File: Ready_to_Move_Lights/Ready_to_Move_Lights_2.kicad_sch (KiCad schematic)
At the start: 42 parts, among them IC1 TLV2371QDBVRQ1, J1 PET-02-XX-X-VT-LC, J2 776280-1, K1 VORA1150-X017T, Q1 IRLZ44N, U1 LM393LVQDDFRQ1, U2 PAMC0381D10QDFXRQ1, U3 NE555D

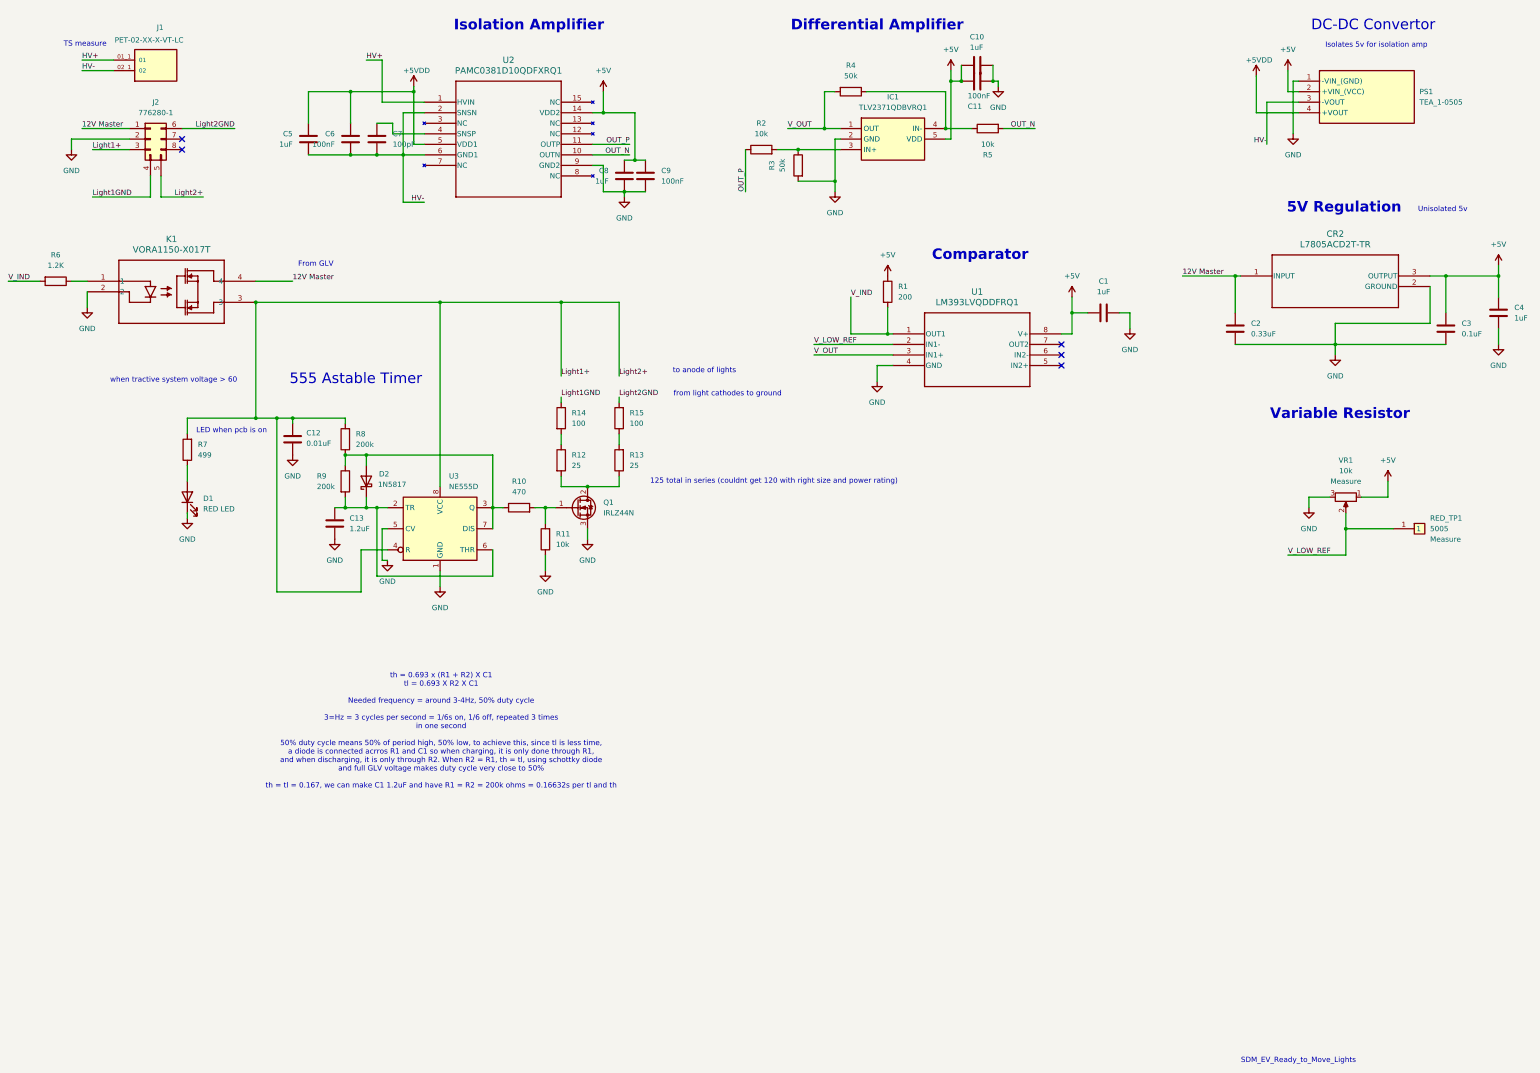
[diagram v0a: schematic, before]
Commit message: Ready_to_Move_Lights Changes
Fixed accidental wiring on 555 output, changed lights' resistors, compressed whole PCB, improved decoupling cap placement
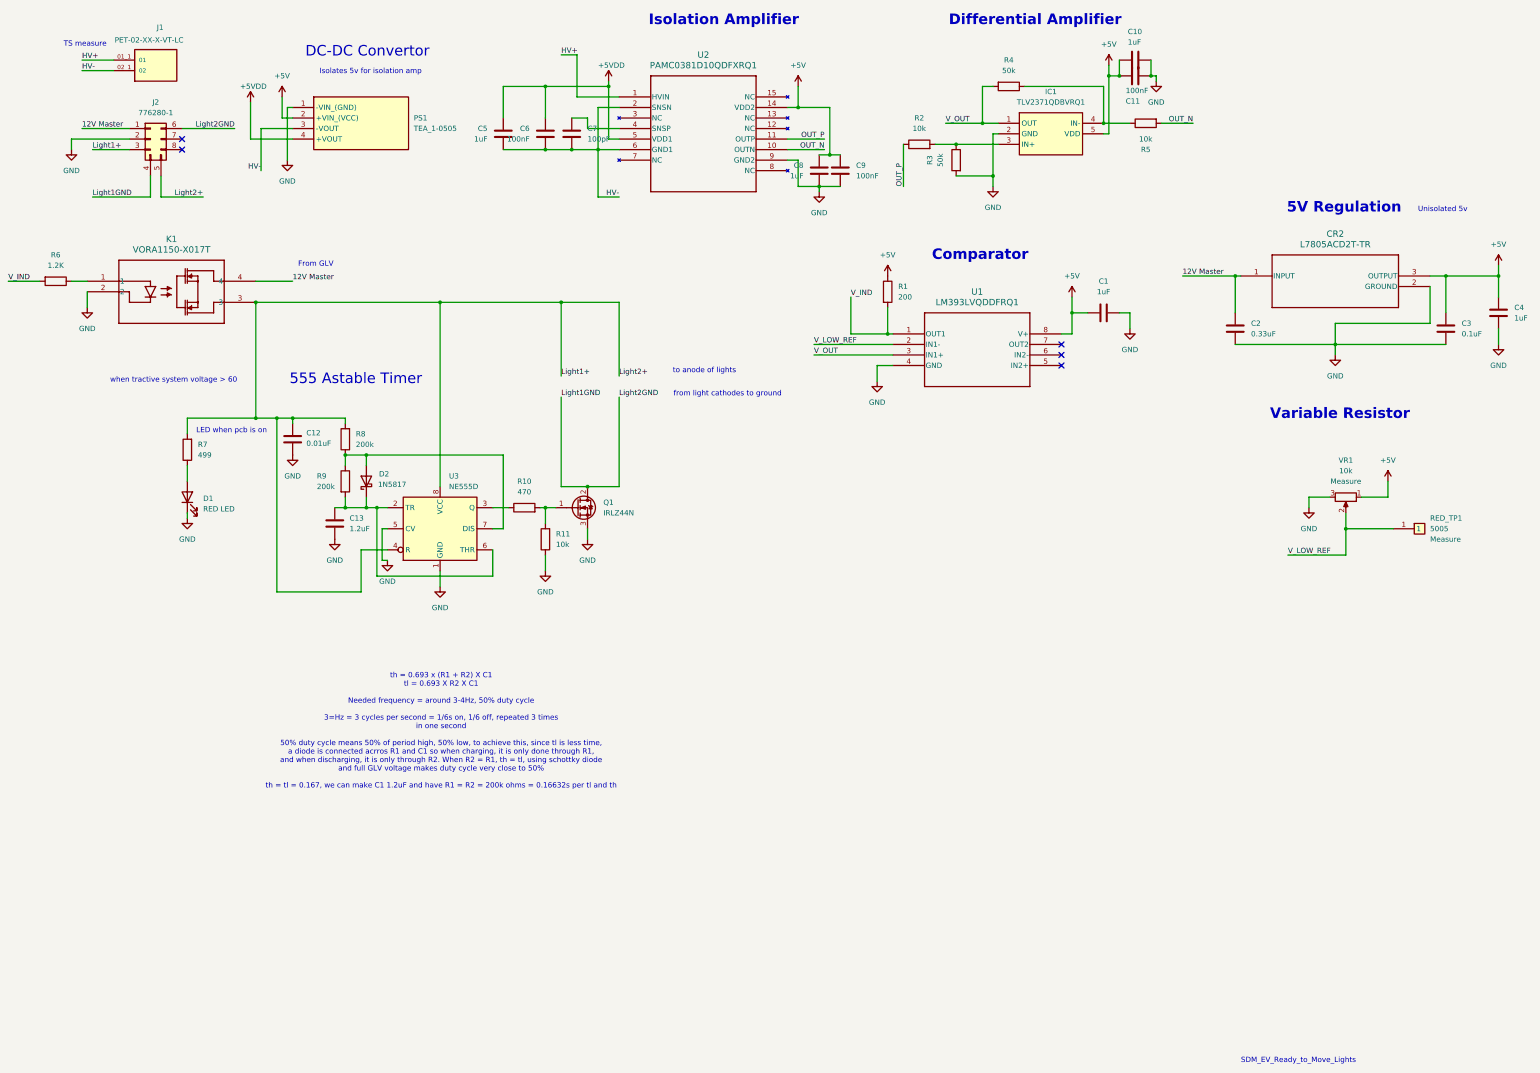
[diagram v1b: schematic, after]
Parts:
- removed R12, R13: 25, Resistor_SMD:R_0603_1608Metric, symbol Device:R
- removed R14, R15: 100, Resistor_SMD:R_0603_1608Metric, symbol Device:R
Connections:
- net Light2GND is gone; now on net Light1GND: J2.6 (Pin_6)
- net Light1GND: now also Q1.2 (D)
- net at D2.2 (A), R8.1, R9.1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: no longer R10.1, U3.3 (Q)
- new net: R10.1, U3.3 (Q)
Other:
- note removed: "125 total in series (couldnt get 120 with right size and power rating)"
- moved on the sheet: C10, C11, C5, C6, C7, C8, C9, IC1, PS1, R10, R2, R3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
